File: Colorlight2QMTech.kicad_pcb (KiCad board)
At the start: 4 copper layers, 66 x 100.5 mm, 25 parts, among them CN1 1473005-4, J1 Conn_02x32_Odd_Even, J2 Conn_02x32_Odd_Even, J3 Connector_USB_C_Receptacle_US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, J4 Conn_01x04_Male, J4-GND1 Conn_01x01_Male, U1 AMS1117-3.3

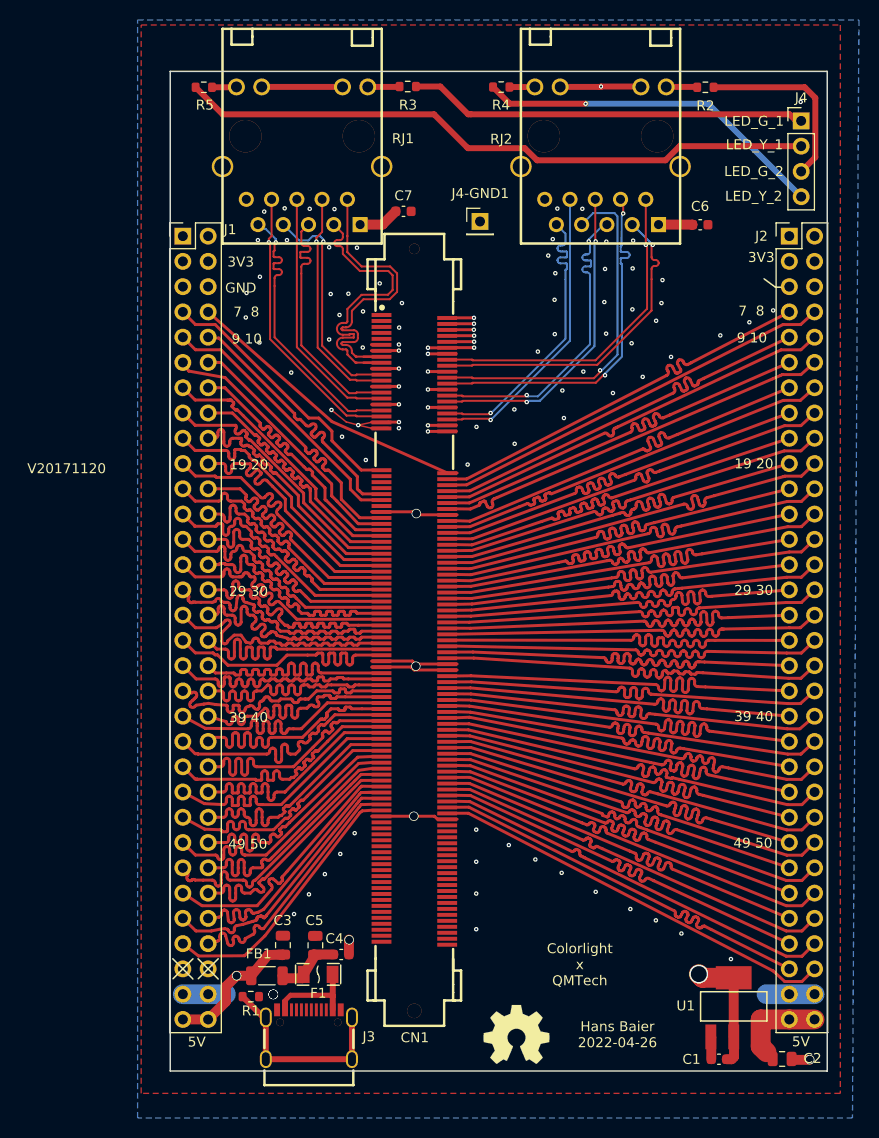
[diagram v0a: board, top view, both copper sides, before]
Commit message: make track widths a bit smaller to satisfy .105mm spacing
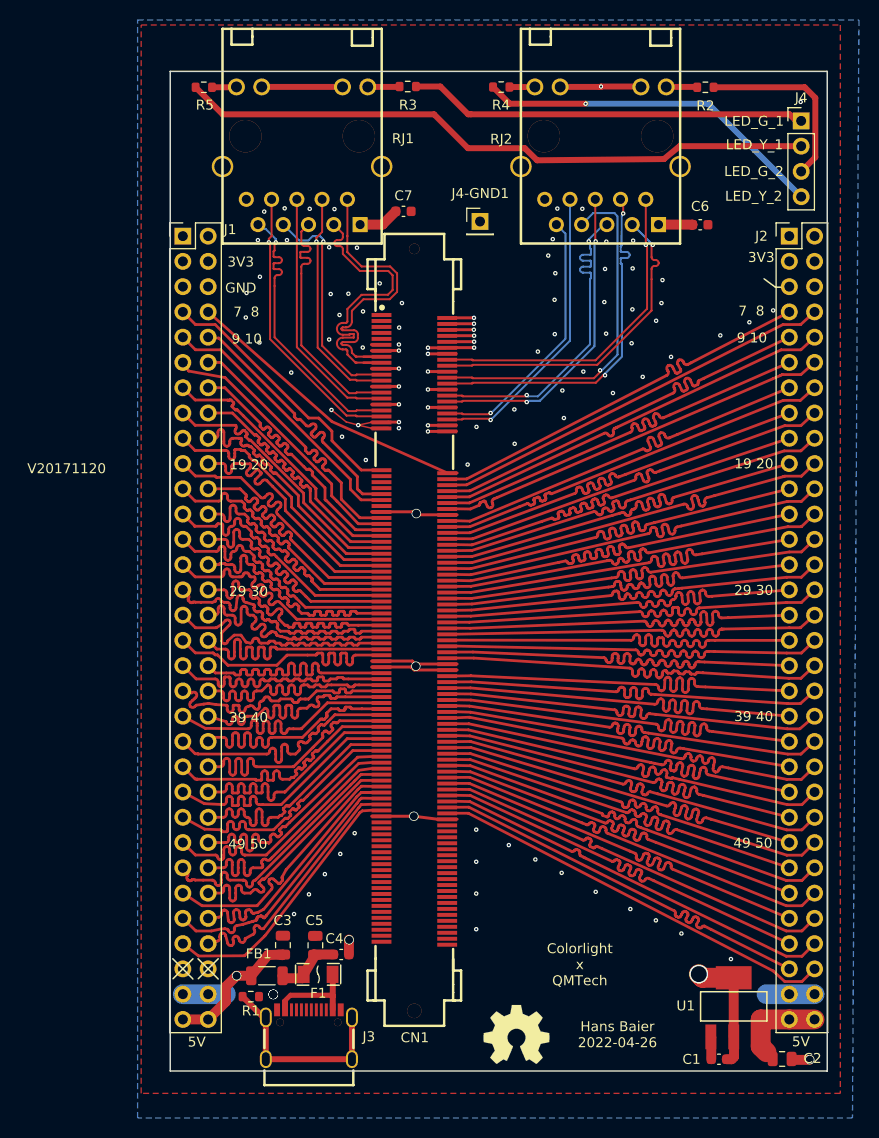
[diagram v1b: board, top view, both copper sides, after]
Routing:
- net /eth2_4-: track 29.8 -> 26.9 mm
- net /eth2_3+: track 32.0 -> 33.5 mm

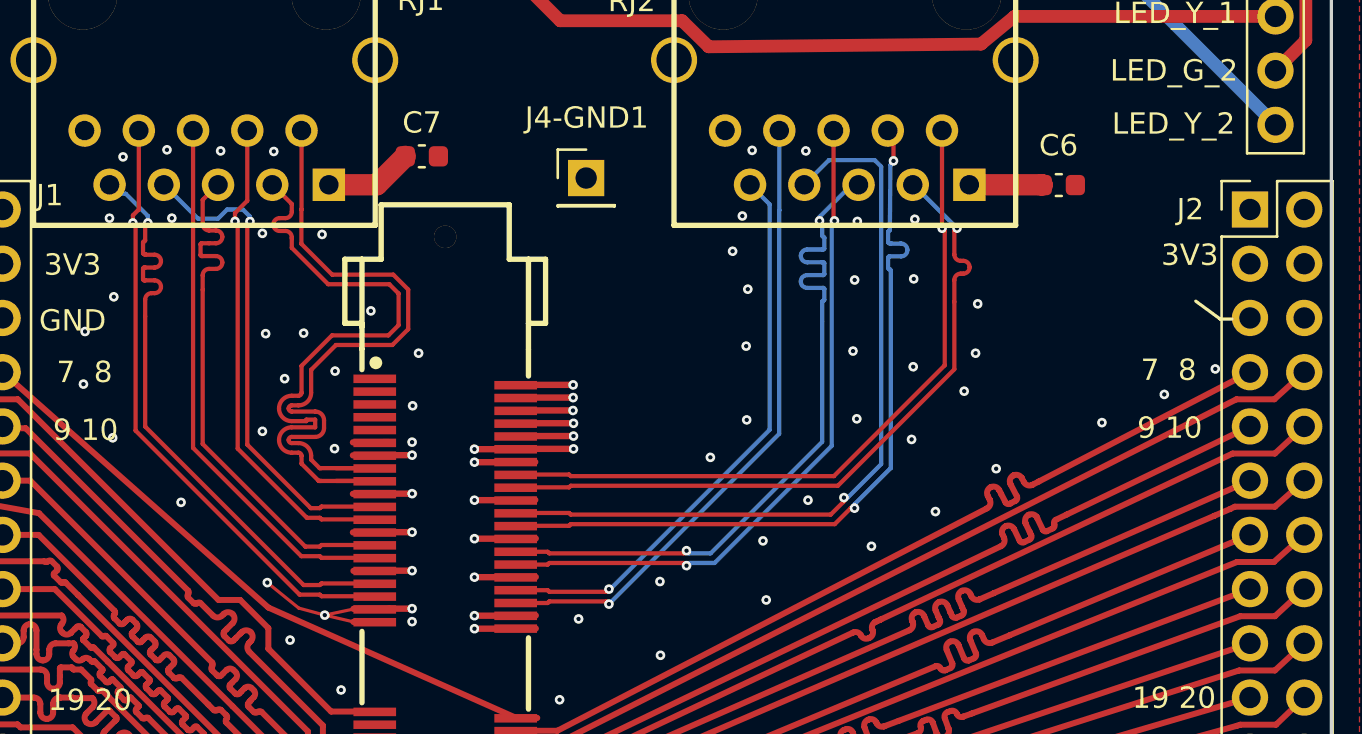
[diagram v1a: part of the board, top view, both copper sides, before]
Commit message: remove unnecessary copper fill and fix silk screen
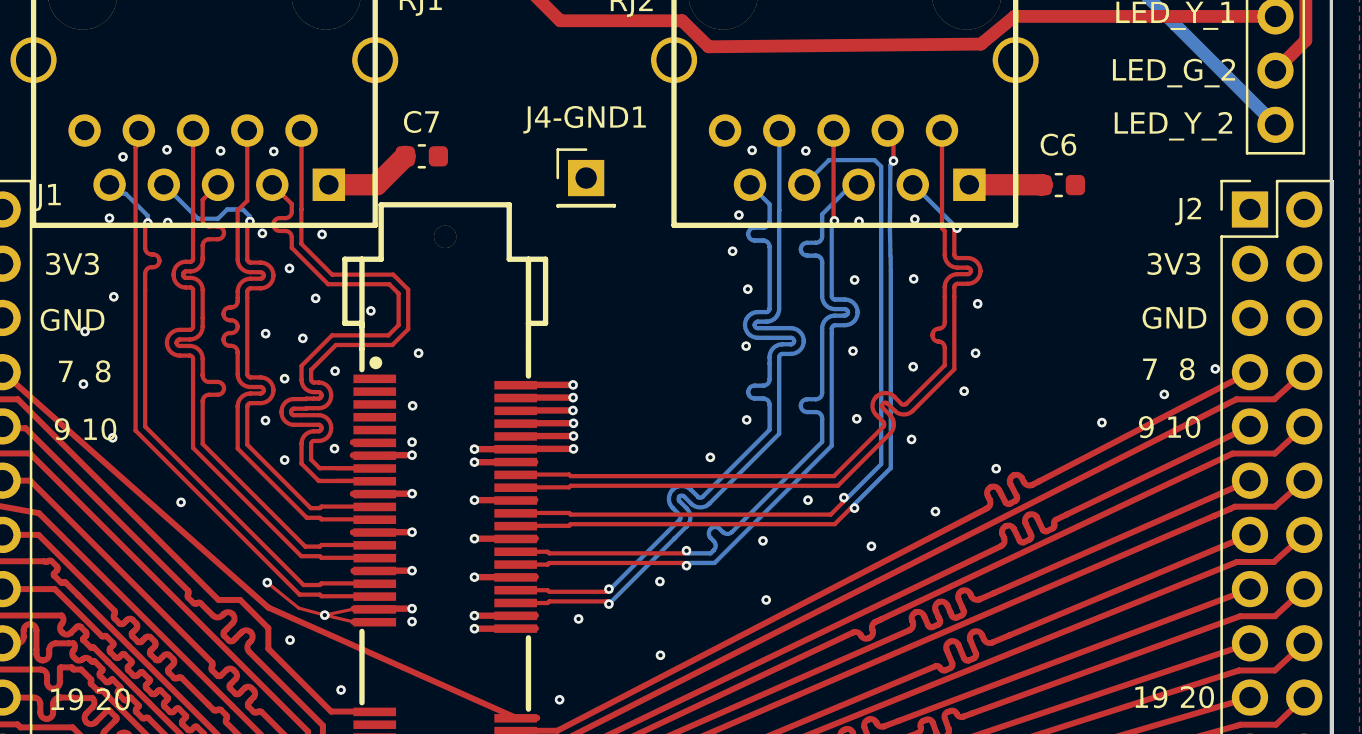
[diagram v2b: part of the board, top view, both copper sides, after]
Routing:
- net /eth2_4-: track 26.9 -> 35.1 mm
- net /eth2_4+: track 29.9 -> 35.2 mm
- net /eth1_2+: track 22.0 -> 26.9 mm, vias 1 -> 0
- net /eth2_1+: track 32.3 -> 36.4 mm, vias 1 -> 0
- net /eth1_2-: track 22.0 -> 25.5 mm
- net /eth1_3-: track 24.5 -> 27.4 mm
- net /eth1_3+: track 24.5 -> 27.3 mm
- net /eth2_1-: track 32.3 -> 34.9 mm
- net /eth1_4-: track 27.7 -> 26.0 mm
- net /eth2_3-: track 32.0 -> 33.8 mm
- net /eth2_3+: track 33.5 -> 35.2 mm, vias 2 -> 1
- net /eth2_2+: track 35.3 -> 33.8 mm
- net /eth1_4+: track 27.9 -> 27.8 mm, vias 1 -> 0
- net GND: vias 98 -> 101

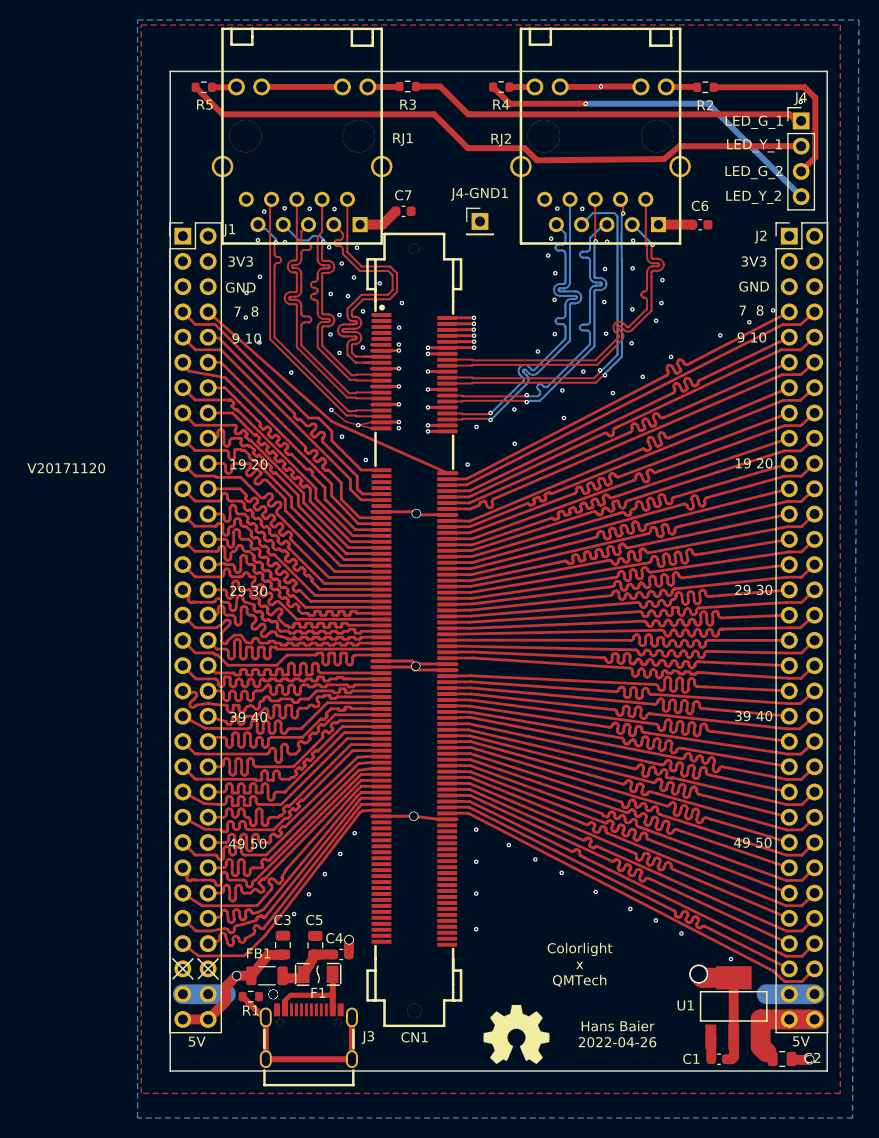
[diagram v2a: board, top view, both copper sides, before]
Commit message: add variant with horizontal SODIMM connector and ethernet
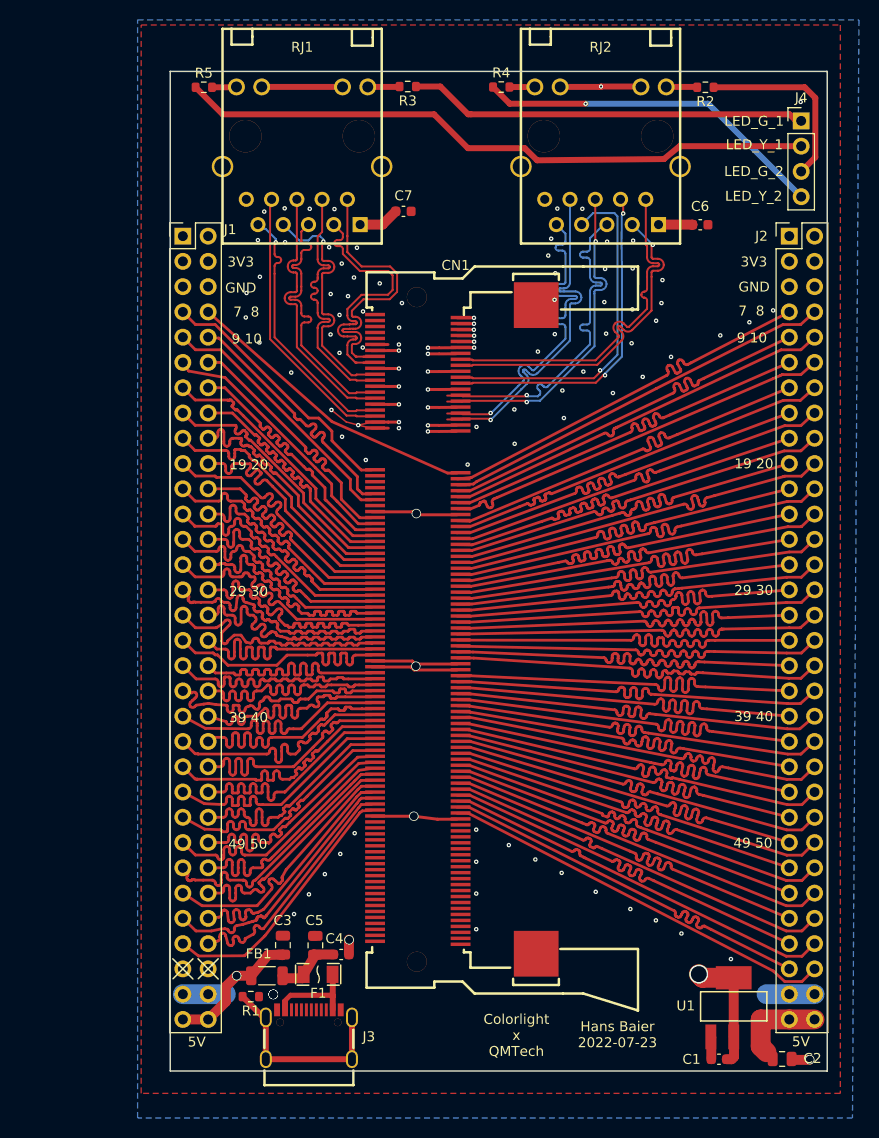
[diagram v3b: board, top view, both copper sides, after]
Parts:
- removed J4-GND1: Conn_01x01_Male, Connector_PinHeader_2.54mm:PinHeader_1x01_P2.54mm_Vertical
- removed N1: OHWLOGO, Symbols:OSHW-Symbol_6.7x6mm_SilkScreen
- removed N2: V20171120, SquantorLabels:Label_version
- CN1: footprint easyeda2kicad:DIMM-SMD_DM-7D4-H2500-M -> easyeda2kicad:SO-DIMM-SMD_200P-P0.60_1473005-4
- moved CN1 4.15 mm to (122.7, 81.7), turned to 0 degrees
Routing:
- net /U1: track 40.3 -> 40.9 mm
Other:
- board text added: "Hans Baier 2022-07-23"
- board text removed: "Hans Baier 2022-04-26"
